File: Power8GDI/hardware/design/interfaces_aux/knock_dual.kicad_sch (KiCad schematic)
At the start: 23 parts, among them U1701 TPIC8101DWR, U1702 SN74AHCT244QPWRQ1, U1703 CLVC1G125QDBVRQ1, Y1701 ASEM1-8.000MHZ-LC-T

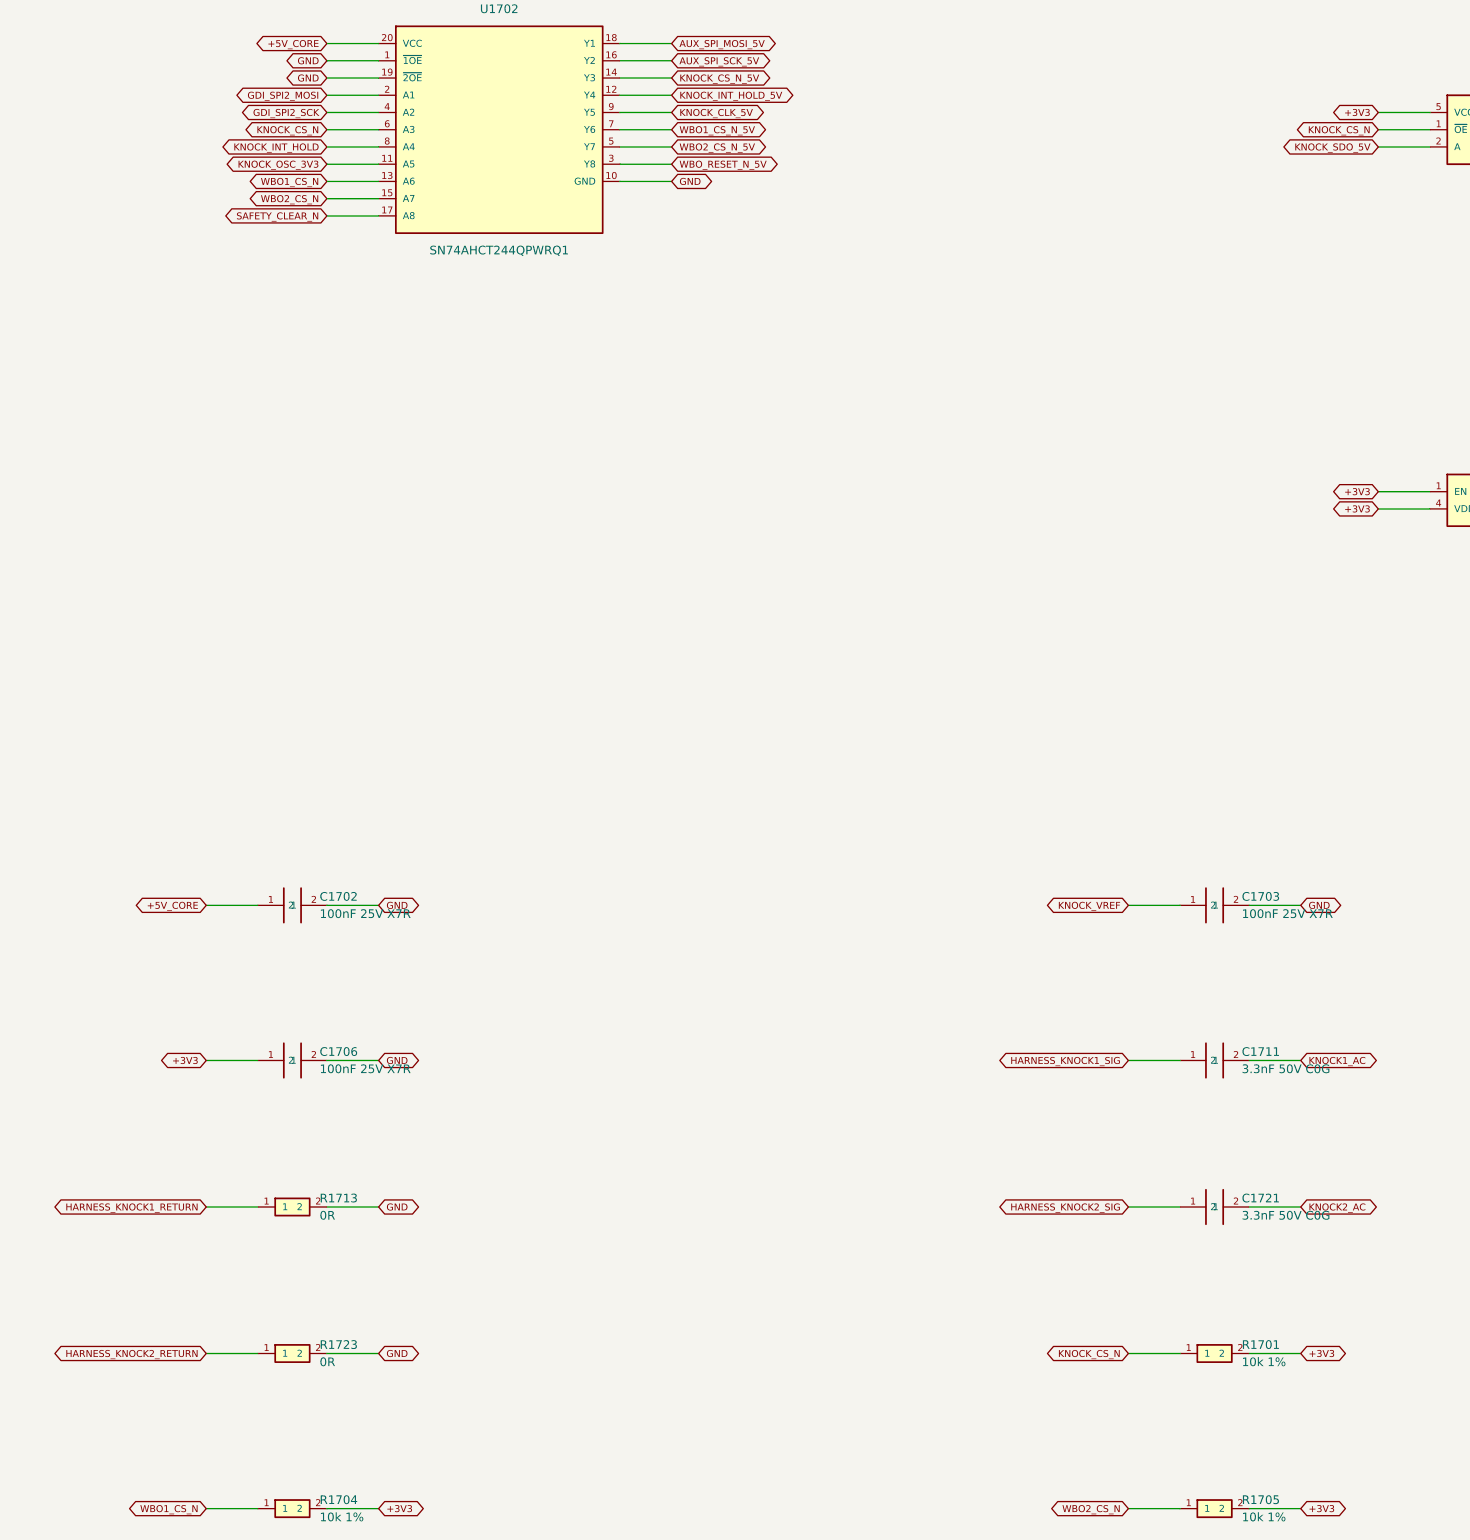
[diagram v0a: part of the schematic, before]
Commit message: Integrate protected GDI and CAN wideband nodes with Huge channel allocation
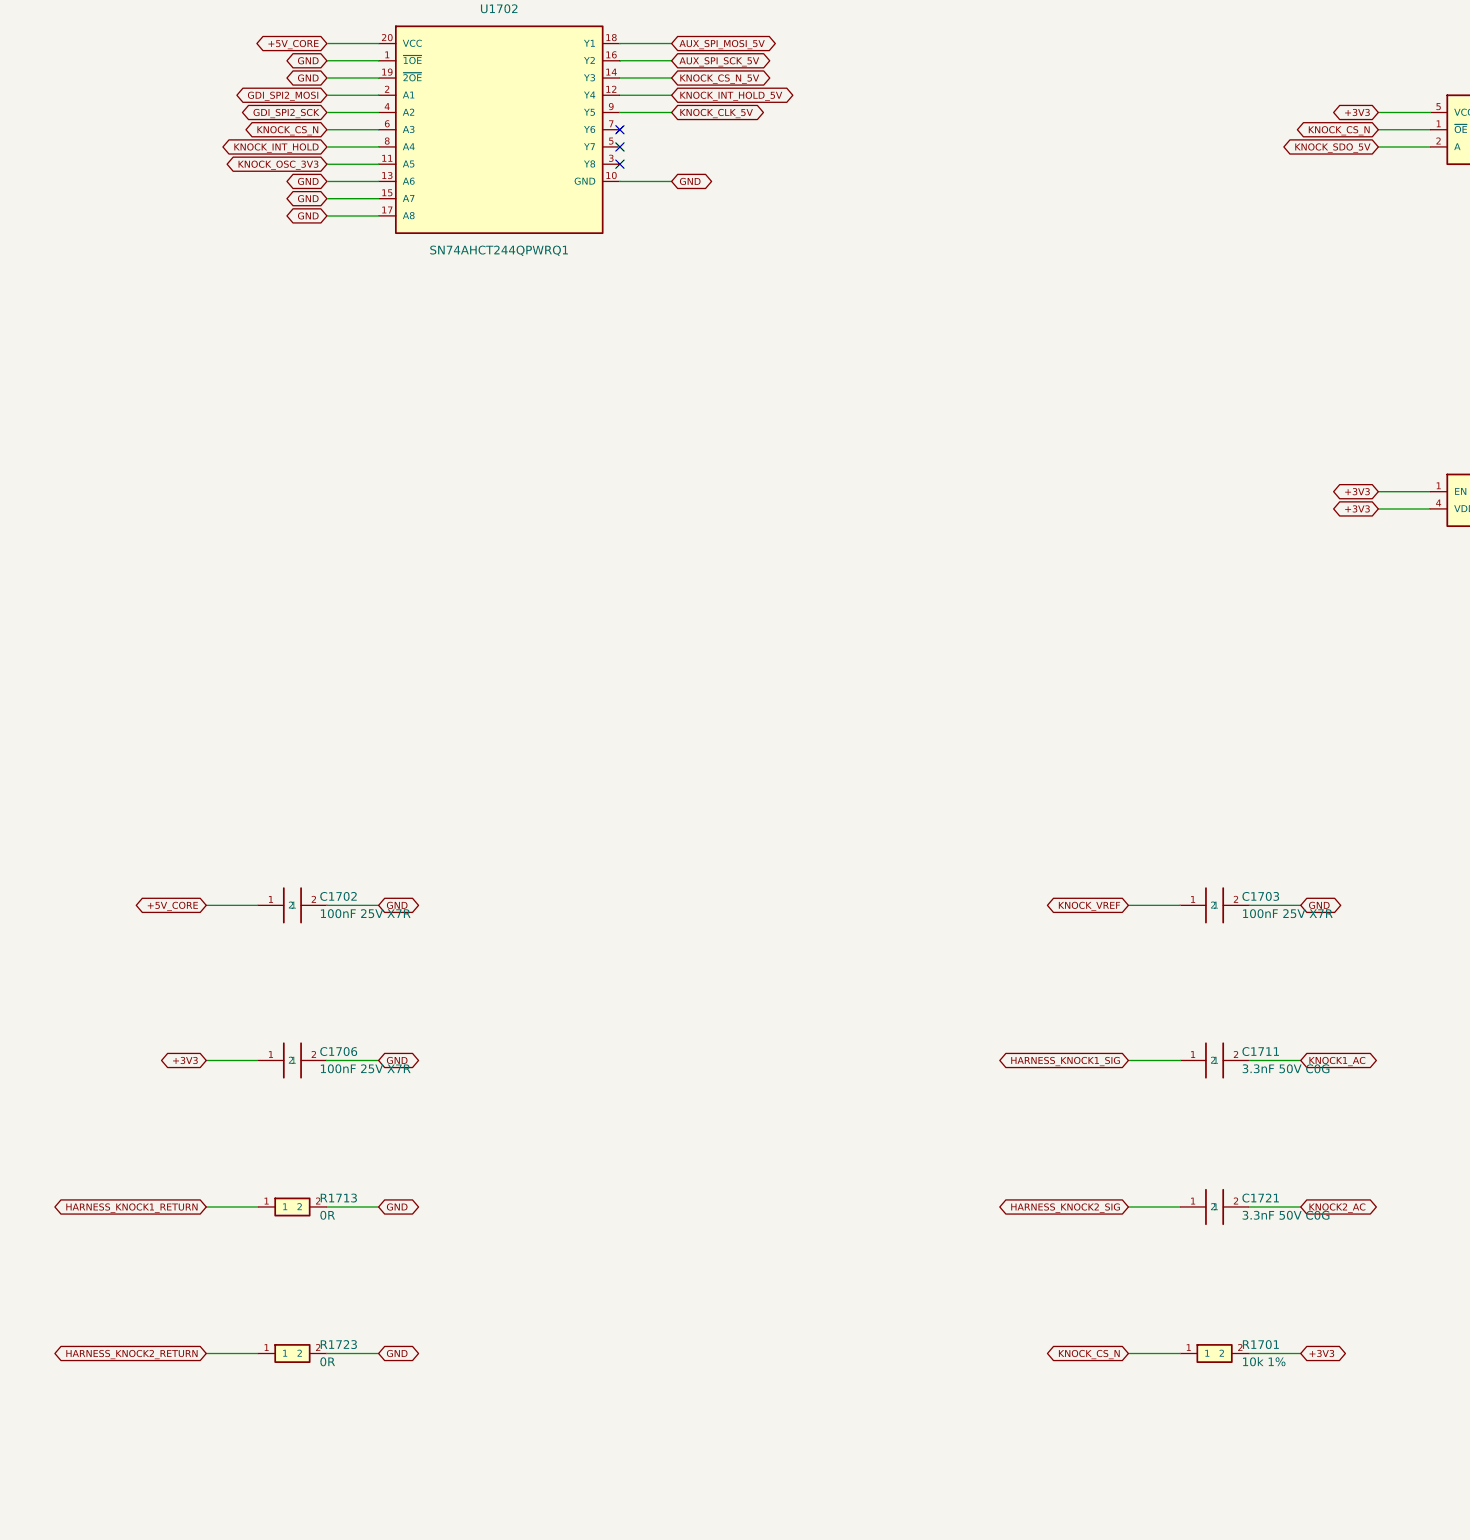
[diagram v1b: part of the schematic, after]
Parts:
- removed R1704, R1705: 10k 1%, Resistor_SMD:R_0603_1608Metric, symbol Power8GDI_Aux:R
- U1702: Design note TTL VIH2V recognizes3.3V; all8 outputs used. Startup/partia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 -> TTL VIH2V recognizes3.3V; five knock/SPI outputs used, unus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
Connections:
- net SAFETY_CLEAR_N is gone; now on net GND: U1702.17 (A8)
- net WBO1_CS_N is gone; now on net GND: U1702.13 (A6)
- net WBO2_CS_N is gone; now on net GND: U1702.15 (A7)
- net WBO1_CS_N_5V: no longer names the net of U1702.7 (Y6)
- net WBO2_CS_N_5V: no longer names the net of U1702.5 (Y7)
- net WBO_RESET_N_5V: no longer names the net of U1702.3 (Y8)
- no-connect marks 5 -> 8
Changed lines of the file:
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@@
 (global_label "AUX_SPI_SCK_5V" (shape bidirectional) (at 105.41 100.33 180) (effects (font (size 1.016 1.016)) (justify left bottom)))
 (no_connect (at 97.79 102.87))
-(symbol (lib_id "Power8GDI_Aux:SN74AHCT244QPWRQ1") (at 234.95 90.17 0) (unit 1) (in_bom yes) (on_board yes) (dnp no) (property "Reference" "U1702" (at 234.95 72.39 0) (effects (font (size 1.27 1.27)))) (property "Value" "SN74AHCT244QPWRQ1" (at 234.95 107.95 0) (effects (font (size 1.27 1.27)))) (property "Footprint" "Package_SO:Texas_PW0020A_TSSOP-20_4.4x6.5mm_P0.65mm" (at 234.95 90.17 0) (effects (font (size 1.27 1.27)) (hide yes))) (property "Design note" "TTL VIH2V recognizes3.3V; all8 outputs used. Startup/partial power still require validation" (at 234.95 90.17 0) (effects (font (size 1.27 1.27)) (hide yes))) (pin "20") (pin "1") (pin "19") (pin "2") (pin "4") (pin "6") (pin "8") (pin "11") (pin "13") (pin "15") (pin "17") (pin "18") (pin "16") (pin "14") (pin "12") (pin "9") (pin "7") (pin "5") (pin "3") (pin "10") (instances (project "Power8GDI_Core" (path "/f4d21065-0a5b-5086-a08e-1af9469f04bd/8965976b-faa0-5281-9f71-542877bfa52b" (reference "U1702") (unit 1))) (project "knock_dual" (path "/20465974-d3b0-5bf0-9403-bb1282024aae" (reference "U1702") (unit 1)))))
+(symbol (lib_id "Power8GDI_Aux:SN74AHCT244QPWRQ1") (at 234.95 90.17 0) (unit 1) (in_bom yes) (on_board yes) (dnp no) (property "Reference" "U1702" (at 234.95 72.39 0) (effects (font (size 1.27 1.27)))) (property "Value" "SN74AHCT244QPWRQ1" (at 234.95 107.95 0) (effects (font (size 1.27 1.27)))) (property "Footprint" "Package_SO:Texas_PW0020A_TSSOP-20_4.4x6.5mm_P0.65mm" (at 234.95 90.17 0) (effects (font (size 1.27 1.27)) (hide yes))) (property "Design note" "TTL VIH2V recognizes3.3V; five knock/SPI outputs used, unused inputs tied low. WBO now uses independent CAN nodes" (at 234.95 90.17 0) (effects (font (size 1.27 1.27)) (hide yes))) (pin "20") (pin "1") (pin "19") (pin "2") (pin "4") (pin "6") (pin "8") (pin "11") (pin "13") (pin "15") (pin "17") (pin "18") (pin "16") (pin "14") (pin "12") (pin "9") (pin "7") (pin "5") (pin "3") (pin "10") (instances (project "Power8GDI_Core" (path "/f4d21065-0a5b-5086-a08e-1af9469f04bd/8965976b-faa0-5281-9f71-542877bfa52b" (reference "U1702") (unit 1))) (project "knock_dual" (path "/20465974-d3b0-5bf0-9403-bb1282024aae" (reference "U1702") (unit 1)))))
 (wire (pts (xy 217.17 77.47) (xy 209.55 77.47)) (stroke (width 0) (type default)))
 (global_label "+5V_CORE" (shape bidirectional) (at 209.55 77.47 0) (effects (font (size 1.016 1.016)) (justify right bottom)))
@@
 (global_label "KNOCK_OSC_3V3" (shape bidirectional) (at 209.55 95.25 0) (effects (font (size 1.016 1.016)) (justify right bottom)))
 (wire (pts (xy 217.17 97.79) (xy 209.55 97.79)) (stroke (width 0) (type default)))
-(global_label "WBO1_CS_N" (shape bidirectional) (at 209.55 97.79 0) (effects (font (size 1.016 1.016)) (justify right bottom)))
+(global_label "GND" (shape bidirectional) (at 209.55 97.79 0) (effects (font (size 1.016 1.016)) (justify right bottom)))
 (wire (pts (xy 217.17 100.33) (xy 209.55 100.33)) (stroke (width 0) (type default)))
-(global_label "WBO2_CS_N" (shape bidirectional) (at 209.55 100.33 0) (effects (font (size 1.016 1.016)) (justify right bottom)))
+(global_label "GND" (shape bidirectional) (at 209.55 100.33 0) (effects (font (size 1.016 1.016)) (justify right bottom)))
 (wire (pts (xy 217.17 102.87) (xy 209.55 102.87)) (stroke (width 0) (type default)))
-(global_label "SAFETY_CLEAR_N" (shape bidirectional) (at 209.55 102.87 0) (effects (font (size 1.016 1.016)) (justify right bottom)))
+(global_label "GND" (shape bidirectional) (at 209.55 102.87 0) (effects (font (size 1.016 1.016)) (justify right bottom)))
 (wire (pts (xy 252.73 77.47) (xy 260.35 77.47)) (stroke (width 0) (type default)))
 (global_label "AUX_SPI_MOSI_5V" (shape bidirectional) (at 260.35 77.47 180) (effects (font (size 1.016 1.016)) (justify left bottom)))
@@
 (wire (pts (xy 252.73 87.63) (xy 260.35 87.63)) (stroke (width 0) (type default)))
 (global_label "KNOCK_CLK_5V" (shape bidirectional) (at 260.35 87.63 180) (effects (font (size 1.016 1.016)) (justify left bottom)))
-(wire (pts (xy 252.73 90.17) (xy 260.35 90.17)) (stroke (width 0) (type default)))
-(global_label "WBO1_CS_N_5V" (shape bidirectional) (at 260.35 90.17 180) (effects (font (size 1.016 1.016)) (justify left bottom)))
-(wire (pts (xy 252.73 92.71) (xy 260.35 92.71)) (stroke (width 0) (type default)))
-(global_label "WBO2_CS_N_5V" (shape bidirectional) (at 260.35 92.71 180) (effects (font (size 1.016 1.016)) (justify left bottom)))
-(wire (pts (xy 252.73 95.25) (xy 260.35 95.25)) (stroke (width 0) (type default)))
-(global_label "WBO_RESET_N_5V" (shape bidirectional) (at 260.35 95.25 180) (effects (font (size 1.016 1.016)) (justify left bottom)))
+(no_connect (at 252.73 90.17))
+(no_connect (at 252.73 92.71))
+(no_connect (at 252.73 95.25))
 (wire (pts (xy 252.73 97.79) (xy 260.35 97.79)) (stroke (width 0) (type default)))
 (global_label "GND" (shape bidirectional) (at 260.35 97.79 180) (effects (font (size 1.016 1.016)) (justify left bottom)))
@@
 (wire (pts (xy 74.93 293.37) (xy 82.55 293.37)) (stroke (width 0) (type default)))
 (global_label "GND" (shape bidirectional) (at 82.55 293.37 180) (effects (font (size 1.016 1.016)) (justify left bottom)))
-(symbol (lib_id "Power8GDI_Aux:R") (at 204.47 293.37 0) (unit 1) (in_bom yes) (on_board yes) (dnp no) (property "Reference" "R1704" (at 208.47 292.1 0) (effects (font (size 1.27 1.27)) (justify left))) (property "Value" "10k 1%" (at 208.47 294.64 0) (effects (font (size 1.27 1.27)) (justify left))) (property "Footprint" "Resistor_SMD:R_0603_1608Metric" (at 204.47 293.37 0) (effects (font (size 1.27 1.27)) (hide yes))) (property "Design note" "" (at 204.47 293.37 0) (effects (font (size 1.27 1.27)) (hide yes))) (pin "1") (pin "2") (instances (project "Power8GDI_Core" (path "/f4d21065-0a5b-5086-a08e-1af9469f04bd/8965976b-faa0-5281-9f71-542877bfa52b" (reference "R1704") (unit 1))) (project "knock_dual" (path "/20465974-d3b0-5bf0-9403-bb1282024aae" (reference "R1704") (unit 1)))))
-(wire (pts (xy 199.39 293.37) (xy 191.77 293.37)) (stroke (width 0) (type default)))
-(global_label "WBO1_CS_N" (shape bidirectional) (at 191.77 293.37 0) (effects (font (size 1.016 1.016)) (justify right bottom)))
-(wire (pts (xy 209.55 293.37) (xy 217.17 293.37)) (stroke (width 0) (type default)))
-(global_label "+3V3" (shape bidirectional) (at 217.17 293.37 180) (effects (font (size 1.016 1.016)) (justify left bottom)))
-(symbol (lib_id "Power8GDI_Aux:R") (at 340.36 293.37 0) (unit 1) (in_bom yes) (on_board yes) (dnp no) (property "Reference" "R1705" (at 344.36 292.1 0) (effects (font (size 1.27 1.27)) (justify left))) (property "Value" "10k 1%" (at 344.36 294.64 0) (effects (font (size 1.27 1.27)) (justify left))) (property "Footprint" "Resistor_SMD:R_0603_1608Metric" (at 340.36 293.37 0) (effects (font (size 1.27 1.27)) (hide yes))) (property "Design note" "" (at 340.36 293.37 0) (effects (font (size 1.27 1.27)) (hide yes))) (pin "1") (pin "2") (instances (project "Power8GDI_Core" (path "/f4d21065-0a5b-5086-a08e-1af9469f04bd/8965976b-faa0-5281-9f71-542877bfa52b" (reference "R1705") (unit 1))) (project "knock_dual" (path "/20465974-d3b0-5bf0-9403-bb1282024aae" (reference "R1705") (unit 1)))))
-(wire (pts (xy 335.28 293.37) (xy 327.66 293.37)) (stroke (width 0) (type default)))
-(global_label "WBO2_CS_N" (shape bidirectional) (at 327.66 293.37 0) (effects (font (size 1.016 1.016)) (justify right bottom)))
-(wire (pts (xy 345.44 293.37) (xy 353.06 293.37)) (stroke (width 0) (type default)))
-(global_label "+3V3" (shape bidirectional) (at 353.06 293.37 180) (effects (font (size 1.016 1.016)) (justify left bottom)))
 (sheet_instances (path "/" (page "1"))))

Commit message: Review B58 injector power stage and bind selected GDI6 BOM
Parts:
- C1701: Hardware_Qualification (none) -> BOARD_QUALIFICATION_PENDING; MPN (none) -> GMC10X7R475K16NT; Manufacturer (none) -> Cal-Chip Electronics; Procurement_Status (none) -> SELECTED_CATALOG_ITEM; Purchase_Released (none) -> false; Selection_Gaps (none) -> []; Selection_ID (none) -> SEL-541f7eb877a5; Selection_Ratings (none) -> {"capacitance_pf": 4700000, "dc_bias_qualification": "PENDI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; Selection_Source_URLs (none) -> https://www.digikey.com/en/products/detail/cal-chip-electro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
- C1702, C1703, C1704, C1705, C1706: Hardware_Qualification (none) -> BOARD_QUALIFICATION_PENDING; MPN (none) -> C0603C104K5RACTU; Manufacturer (none) -> KEMET; Procurement_Status (none) -> SELECTED_CATALOG_ITEM; Purchase_Released (none) -> false; Selection_Gaps (none) -> []; Selection_ID (none) -> SEL-6bf9727c4e40; Selection_Ratings (none) -> {"capacitance_pf": 100000, "dielectric": "X7R", "rated_volt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; Selection_Source_URLs (none) -> https://search.kemet.com/download/specsheet/C0603C104K5RACTU
- C1711, C1721: Hardware_Qualification (none) -> BOARD_QUALIFICATION_PENDING; MPN (none) -> C0603C332J5GACTU; Manufacturer (none) -> KEMET; Procurement_Status (none) -> SELECTED_CATALOG_ITEM; Purchase_Released (none) -> false; Selection_Gaps (none) -> []; Selection_ID (none) -> SEL-9caf65fb5559; Selection_Ratings (none) -> {"capacitance_pf": 3300, "dielectric": "C0G", "rated_voltag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; Selection_Source_URLs (none) -> https://www.digikey.com/en/products/detail/kemet/C0603C332J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
- R1701, R1702: Hardware_Qualification (none) -> BOARD_QUALIFICATION_PENDING; MPN (none) -> CRCW060310K0FKEA; Manufacturer (none) -> Vishay; Procurement_Status (none) -> SELECTED_FAMILY_CODE; Purchase_Released (none) -> false; Selection_Gaps (none) -> []; Selection_ID (none) -> SEL-9c0806476875; Selection_Ratings (none) -> {"aec_q200": true, "derating": "Use manufacturer power vers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; Selection_Source_URLs (none) -> https://www.vishay.com/docs/20035/dcrcwe3.pdf
- R1703, R1711, R1712, R1721, R1722: Hardware_Qualification (none) -> BOARD_QUALIFICATION_PENDING; MPN (none) -> CRCW0603100KFKEA; Manufacturer (none) -> Vishay; Procurement_Status (none) -> SELECTED_FAMILY_CODE; Purchase_Released (none) -> false; Selection_Gaps (none) -> []; Selection_ID (none) -> SEL-4e3f06cba0aa; Selection_Ratings (none) -> {"aec_q200": true, "derating": "Use manufacturer power vers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; Selection_Source_URLs (none) -> https://www.vishay.com/docs/20035/dcrcwe3.pdf
- R1713, R1723: Hardware_Qualification (none) -> BOARD_QUALIFICATION_PENDING; MPN (none) -> CRCW06030000Z0EA; Manufacturer (none) -> Vishay; Procurement_Status (none) -> SELECTED_FAMILY_CODE; Purchase_Released (none) -> false; Selection_Gaps (none) -> []; Selection_ID (none) -> SEL-8473f02313b2; Selection_Ratings (none) -> {"aec_q200": true, "current_a": 2, "power_reference_tempera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; Selection_Source_URLs (none) -> https://www.vishay.com/docs/20035/dcrcwe3.pdf
- U1701: Hardware_Qualification (none) -> BOARD_STRESS_AND_LAYOUT_REVIEW_REQUIRED; MPN (none) -> TPIC8101DWR; Manufacturer (none) -> Texas Instruments; Procurement_Status (none) -> SELECTED_CONDITIONAL; Purchase_Released (none) -> false; Selection_Gaps (none) -> ["Catalog family limits verified; exact order suffix and ci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; Selection_ID (none) -> SEL-5034de544a46; Selection_Ratings (none) -> {"channels": 2, "interface": "SPI", "supported_clock_mhz": 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; Selection_Source_URLs (none) -> https://www.ti.com/product/TPIC8101
- U1702: Hardware_Qualification (none) -> PINOUT_RATINGS_AND_DELIVERY_SUFFIX_REVIEW_PENDING; MPN (none) -> SN74AHCT244QPWRQ1; Manufacturer (none) -> Texas Instruments; Procurement_Status (none) -> REFERENCE_MPN_RETAINED; Purchase_Released (none) -> false; Selection_Gaps (none) -> ["Existing schematic MPN retained. Complete circuit rating/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; Selection_ID (none) -> SEL-dd1dda416e0b; Selection_Ratings (none) -> {}; Selection_Source_URLs (none) -> https://www.ti.com/product/SN74AHCT244-Q1/part-details/SN74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
- U1703: Hardware_Qualification (none) -> PINOUT_RATINGS_AND_DELIVERY_SUFFIX_REVIEW_PENDING; MPN (none) -> CLVC1G125QDBVRQ1; Manufacturer (none) -> Texas Instruments; Procurement_Status (none) -> REFERENCE_MPN_RETAINED; Purchase_Released (none) -> false; Selection_Gaps (none) -> ["Existing schematic MPN retained. Complete circuit rating/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; Selection_ID (none) -> SEL-19ec20a73a28; Selection_Ratings (none) -> {}; Selection_Source_URLs (none) -> https://www.ti.com/product/SN74LVC1G125-Q1/part-details/CLV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
- Y1701: Hardware_Qualification (none) -> PINOUT_RATINGS_AND_DELIVERY_SUFFIX_REVIEW_PENDING; MPN (none) -> ASEM1-8.000MHZ-LC-T; Manufacturer (none) -> Abracon; Procurement_Status (none) -> REFERENCE_MPN_RETAINED; Purchase_Released (none) -> false; Selection_Gaps (none) -> ["Existing schematic MPN retained. Complete circuit rating/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; Selection_ID (none) -> SEL-4a33baffd848; Selection_Ratings (none) -> {}; Selection_Source_URLs (none) -> https://abracon.com/Oscillators/ASEM.pdf
